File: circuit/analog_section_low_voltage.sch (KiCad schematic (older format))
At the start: 38 parts, among them J2 Screw_Terminal_01x12, K1 Reed Relay DPST NC, Q2 2N2222 or similar, U11 LM7332, U12 LM7332_Power_Supply

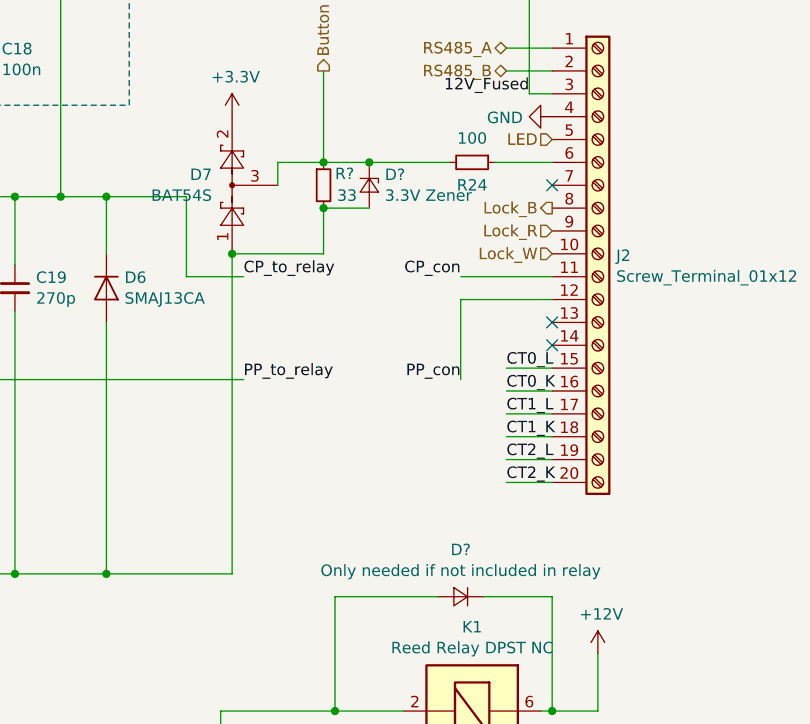
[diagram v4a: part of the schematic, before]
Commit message: Update schematic
Schematic updated with latest changes and preparation for footprint assignment
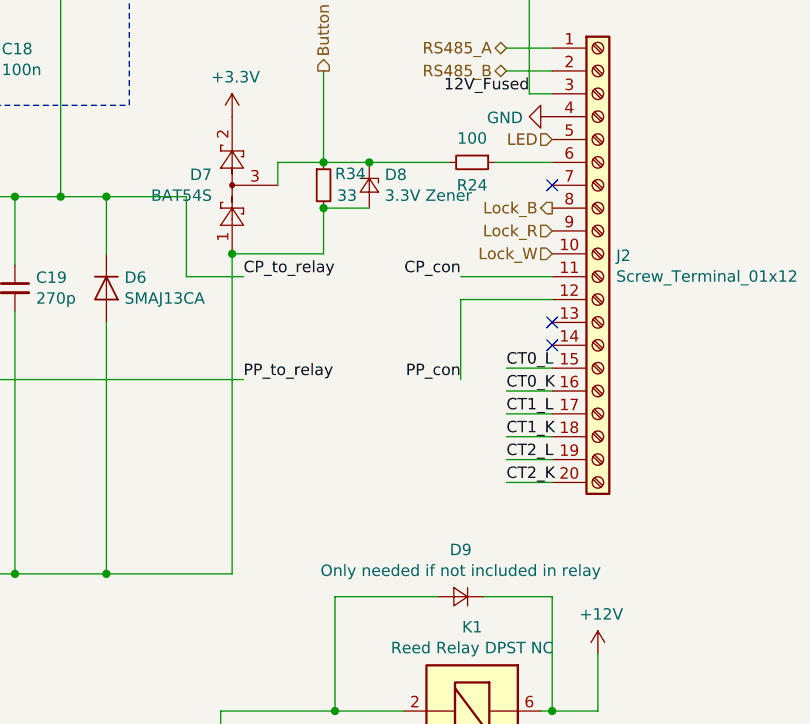
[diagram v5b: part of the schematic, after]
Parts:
- K1: footprint Relay_THT:Relay_StandexMeder_DIP_LowProfile -> (none)
- gave numbers to parts that had none: 3
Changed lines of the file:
@@
 F 0 "K1" V 7483 5400 50  0000 C CNN
 F 1 "Reed Relay DPST NC" V 7574 5400 50  0000 C CNN
-F 2 "Relay_THT:Relay_StandexMeder_DIP_LowProfile" H 8650 5350 50  0001 L CNN
+F 2 "" H 8650 5350 50  0001 L CNN
 F 3 "https://standexelectronics.com/wp-content/uploads/datasheet_reed_relay_DIP.pdf" H 8150 5400 50  0001 C CNN
 	1    8150 5400
@@
 	6200 1150 8400 1150
 $Comp
-L Device:R_Small R?
+L Device:R_Small R34
 U 1 1 5ECD3565
 P 7500 2800
-F 0 "R?" H 7550 2850 50  0000 L CNN
+F 0 "R34" H 7550 2850 50  0000 L CNN
 F 1 "33" H 7559 2755 50  0000 L CNN
 F 2 "" H 7500 2800 50  0001 C CNN
@@
 	7300 2700 7500 2700
 $Comp
-L Device:D_Zener_Small D?
+L Device:D_Zener_Small D8
 U 1 1 5ECE49DD
 P 7700 2800
-F 0 "D?" V 7654 2868 50  0000 L CNN
+F 0 "D8" V 7654 2868 50  0000 L CNN
 F 1 "3.3V Zener" V 7745 2868 50  0000 L CNN
 F 2 "" V 7700 2800 50  0001 C CNN
@@
 12V_Fused
 $Comp
-L Device:D_Small D?
+L Device:D_Small D9
 U 1 1 5ECFD670
 P 8100 4600
-F 0 "D?" H 8100 4395 50  0000 C CNN
+F 0 "D9" H 8100 4395 50  0000 C CNN
 F 1 "Only needed if not included in relay" H 8100 4486 50  0000 C CNN
 F 2 "" V 8100 4600 50  0001 C CNN

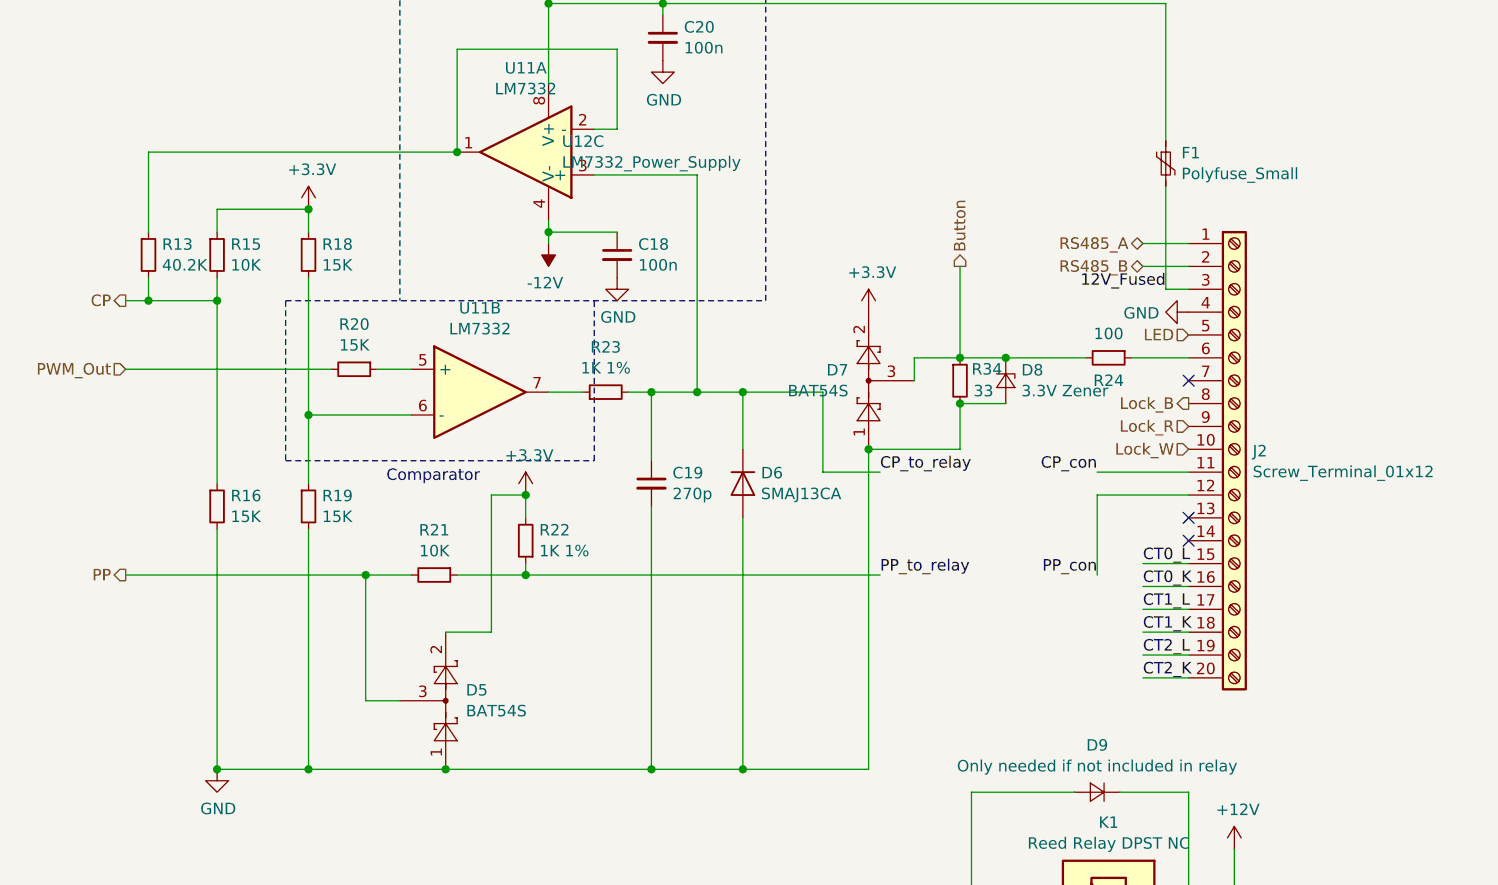
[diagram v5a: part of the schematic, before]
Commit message: Add new component data in schematic
Updated components and footprints in schematic
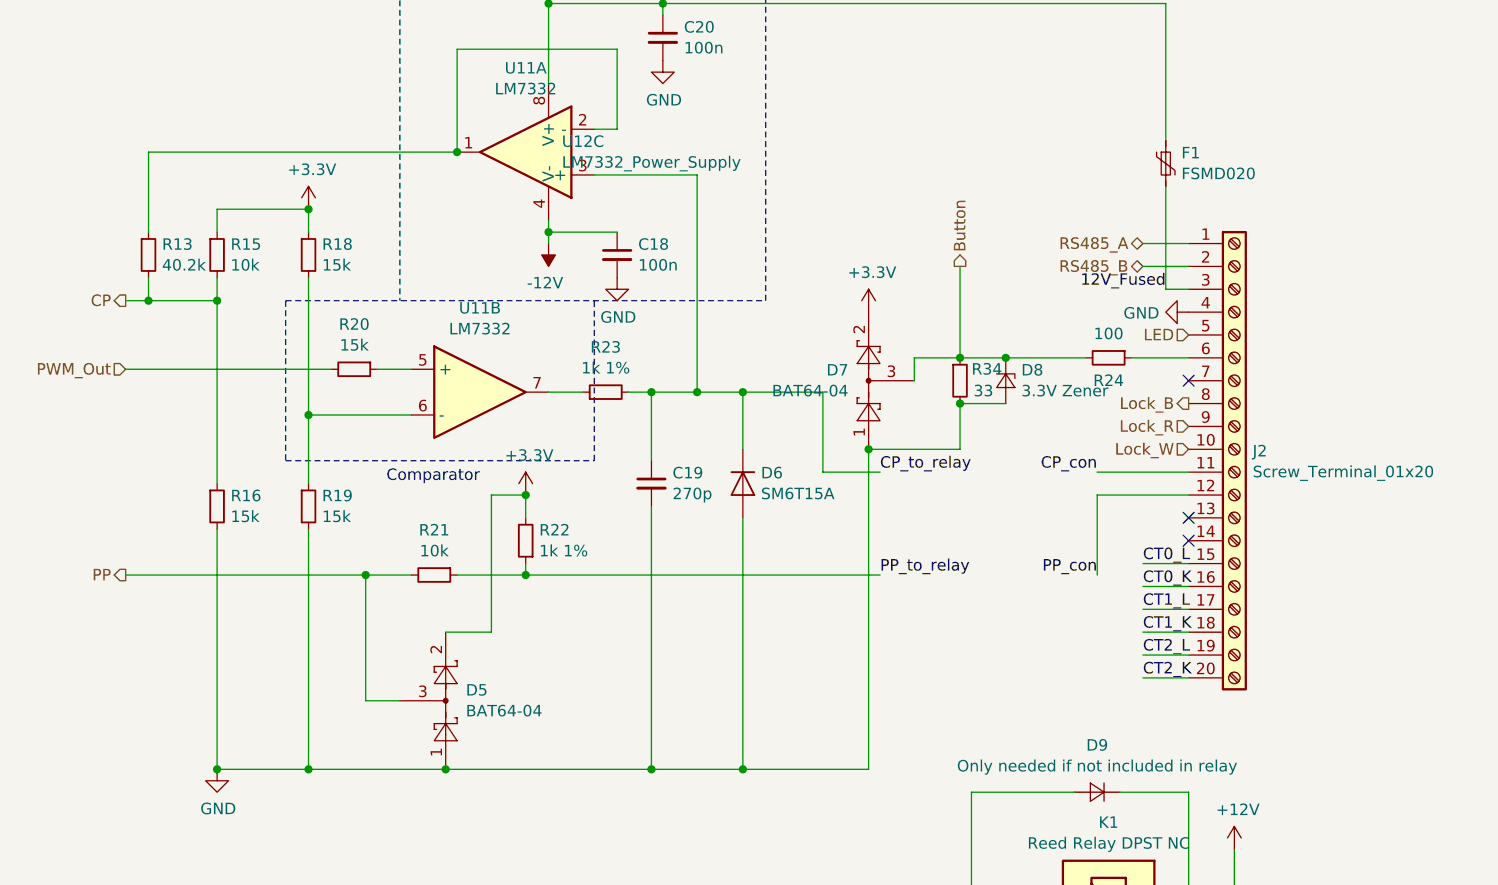
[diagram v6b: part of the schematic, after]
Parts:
- C18, C20, C23, C24, C25: footprint (none) -> Capacitor_SMD:C_0603_1608Metric_Pad1.05x0.95mm_HandSolder; Part (none) -> Kemet C0603C104K3RAC7867+ Keramik-Kondensator SMD 0603 100 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; PartNo (none) -> 1420339; Supplier (none) -> Conrad
- C19: footprint (none) -> Capacitor_SMD:C_0603_1608Metric_Pad1.05x0.95mm_HandSolder; Part (none) -> Yageo CC0603JRNPO9BN271B Keramik-Kondensator SMD 0603 270 p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; PartNo (none) -> 445791; Supplier (none) -> Conrad
- D5, D7: value BAT54S -> BAT64-04; footprint Package_TO_SOT_SMD:SOT-23 -> Package_TO_SOT_SMD:SOT-23_Handsoldering; Part (none) -> Gleichrichter BAT64-04 (Dual) SOT-23-3 40 V Array - 1 Paar 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; PartNo (none) -> 152998; Supplier (none) -> Conrad
- D6: value SMAJ13CA -> SM6T15A; footprint Diode_THT:D_DO-35_SOD27_P7.62mm_Horizontal -> Diode_SMD:D_SMB_Handsoldering; Part (none) -> SM6T15A-E3/52 DO-214AA 14.3 V 600 W; PartNo (none) -> 596320; Supplier (none) -> Conrad
- D8: footprint (none) -> Diode_SMD:D_MiniMELF_Handsoldering; Part (none) -> TC-ZMM3.3 Gehäuseart (Halbleiter) SOD-80C Zener-Spannung 3.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; PartNo (none) -> 1581796; Supplier (none) -> Conrad
- F1: value Polyfuse_Small -> FSMD020; footprint (none) -> Fuse:Fuse_1812_4532Metric_Pad1.30x3.40mm_HandSolder; Part (none) -> ESKA FSMD020 PTC-Sicherung; PartNo (none) -> 524900; Supplier (none) -> Conrad
- J2: value Screw_Terminal_01x12 -> Screw_Terminal_01x20
- R13: value 40.2K -> 40.2k; footprint (none) -> Resistor_SMD:R_0805_2012Metric_Pad1.15x1.40mm_HandSolder; Part (none) -> Panasonic ERJ-6ENF4022V Dickschicht-Widerstand 40.2 kΩ SMD 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; PartNo (none) -> 1480312; Supplier (none) -> Conrad
- R14: footprint (none) -> Resistor_SMD:R_0603_1608Metric_Pad1.05x0.95mm_HandSolder; Part (none) -> TRU COMPONENTS TC-0603SAJ0222T5E203 Dickschicht-Widerstand 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; PartNo (none) -> 1585814; Supplier (none) -> Conrad
- R15, R21: value 10K -> 10k; footprint (none) -> Resistor_SMD:R_0603_1608Metric_Pad1.05x0.95mm_HandSolder; Part (none) -> TRU COMPONENTS TC-0603SAF1002T5E203 Dickschicht-Widerstand 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; PartNo (none) -> 1585269; Supplier (none) -> Conrad
- R16, R18, R19, R20: value 15K -> 15k; footprint (none) -> Resistor_SMD:R_0603_1608Metric_Pad1.05x0.95mm_HandSolder; Part (none) -> TRU COMPONENTS TC-0603SAJ0153T5E203 Dickschicht-Widerstand 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; PartNo (none) -> 1585827; Supplier (none) -> Conrad
- R17: footprint (none) -> Resistor_SMD:R_0603_1608Metric_Pad1.05x0.95mm_HandSolder; Part (none) -> TRU COMPONENTS TC-HP03W5F2202T5E203 Dickschicht-Widerstand 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; PartNo (none) -> 1584163; Supplier (none) -> Conrad
- R22, R23: value 1K 1% -> 1k 1%; footprint (none) -> Resistor_SMD:R_0603_1608Metric_Pad1.05x0.95mm_HandSolder; Part (none) -> TRU COMPONENTS TC-HP03W5F1001T5E203 Dickschicht-Widerstand 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; PartNo (none) -> 1585508; Supplier (none) -> Conrad
- R24, R28, R29, R30: footprint (none) -> Resistor_SMD:R_0603_1608Metric_Pad1.05x0.95mm_HandSolder; Part (none) -> TRU COMPONENTS TC-0603SAJ0101T5E203 Dickschicht-Widerstand 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; PartNo (none) -> 1583838; Supplier (none) -> Conrad
- R26, R27: footprint (none) -> Resistor_SMD:R_0603_1608Metric_Pad1.05x0.95mm_HandSolder; Part (none) -> TRU COMPONENTS TC-0603SAF1002T5E203 Dickschicht-Widerstand 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; PartNo (none) -> 1585269; Supplier (none) -> Conrad
- R31, R32, R33: footprint (none) -> Resistor_SMD:R_0603_1608Metric_Pad1.05x0.95mm_HandSolder; Part (none) -> TRU COMPONENTS TC-0603SAJ0220T5E203 Dickschicht-Widerstand 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; PartNo (none) -> 1585778; Supplier (none) -> Conrad
- R34: footprint (none) -> Resistor_SMD:R_0603_1608Metric_Pad1.05x0.95mm_HandSolder; Part (none) -> TRU COMPONENTS TC-0603SAJ0330T5E203 Dickschicht-Widerstand 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; PartNo (none) -> 1584262; Supplier (none) -> Conrad
